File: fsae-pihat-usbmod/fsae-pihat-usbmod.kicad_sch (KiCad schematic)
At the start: 4 parts, among them J1 Conn_01x03_Socket, J2 PDC004 V2 PD Trigger, U1 MT3608 Boost

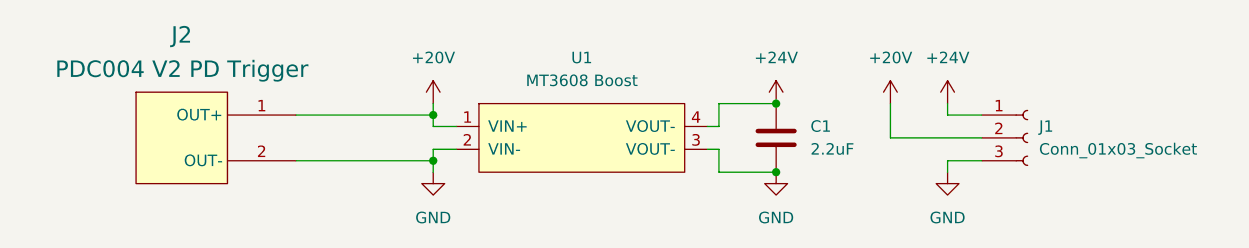
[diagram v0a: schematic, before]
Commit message: fix: missed hat pullup; feat: new pd module
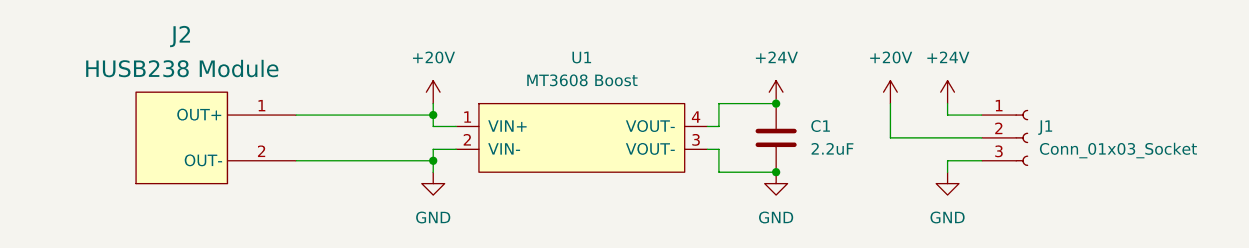
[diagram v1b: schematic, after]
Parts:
- removed J2: PDC004 V2 PD Trigger, PDC004-Footprint, symbol custom:PDC004
- added J2: HUSB238 Module, HUSB238_module, symbol custom:HUSB238_module
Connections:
- net +20V: now also J2.1 (OUT+)
- net GND: now also J2.2 (OUT-)
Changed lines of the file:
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@@
 	)
 	(symbol
-		(lib_id "custom:PDC004")
+		(lib_id "custom:HUSB238_module")
 		(at 109.22 96.52 90)
 		(unit 1)
@@
 			)
 		)
-		(property "Value" "PDC004 V2 PD Trigger"
+		(property "Value" "HUSB238 Module"
 			(at 109.22 88.9 90)
 			(effects
@@
 			)
 		)
-		(property "Footprint" "PDC004-Footprint"
+		(property "Footprint" "HUSB238_module"
 			(at 109.22 96.52 0)
 			(effects
@@
 			)
 		)
-		(property "Datasheet" ""
+		(property "Datasheet" "https://www.aliexpress.com/item/1005008369234535.html"
 			(at 109.22 96.52 0)
 			(effects
@@
 			)
 		)
-		(property "Description" "Fixed Voltage 20V PDC004 (NEW REV w/ HT50 regulator) USB-C PD Trigger from Aliexpress"
+		(property "Description" "Adjustable 20V Default Purple SMT HUSB238 USB-C PD Trigger from Aliexpress"
 			(at 109.22 96.52 0)
 			(effects
@@
 			)
 		)
+		(pin "2"
+		)
 		(pin "1"
 		)
-		(pin "2"
-		)
 		(instances

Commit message: fix: usb module fp + pcb
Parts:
- J2: footprint HUSB238_module -> custom:HUSB238_module_purple
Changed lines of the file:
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@@
 			)
 		)
-		(property "Footprint" "HUSB238_module"
+		(property "Footprint" "custom:HUSB238_module_purple"
 			(at 109.22 96.52 0)
 			(effects
